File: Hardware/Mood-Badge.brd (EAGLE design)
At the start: 100 x 80 mm, 0 parts

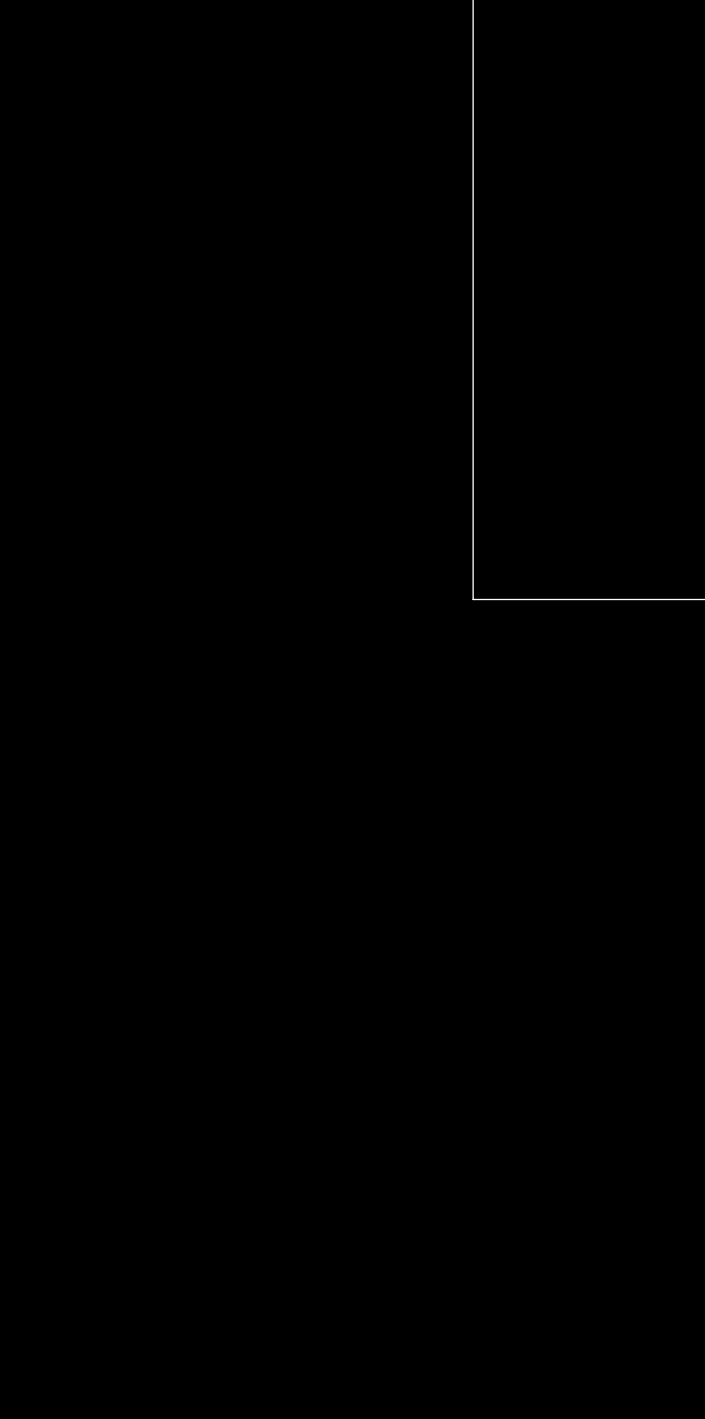
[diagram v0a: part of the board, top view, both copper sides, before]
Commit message: atmega schematics is now establish/included.
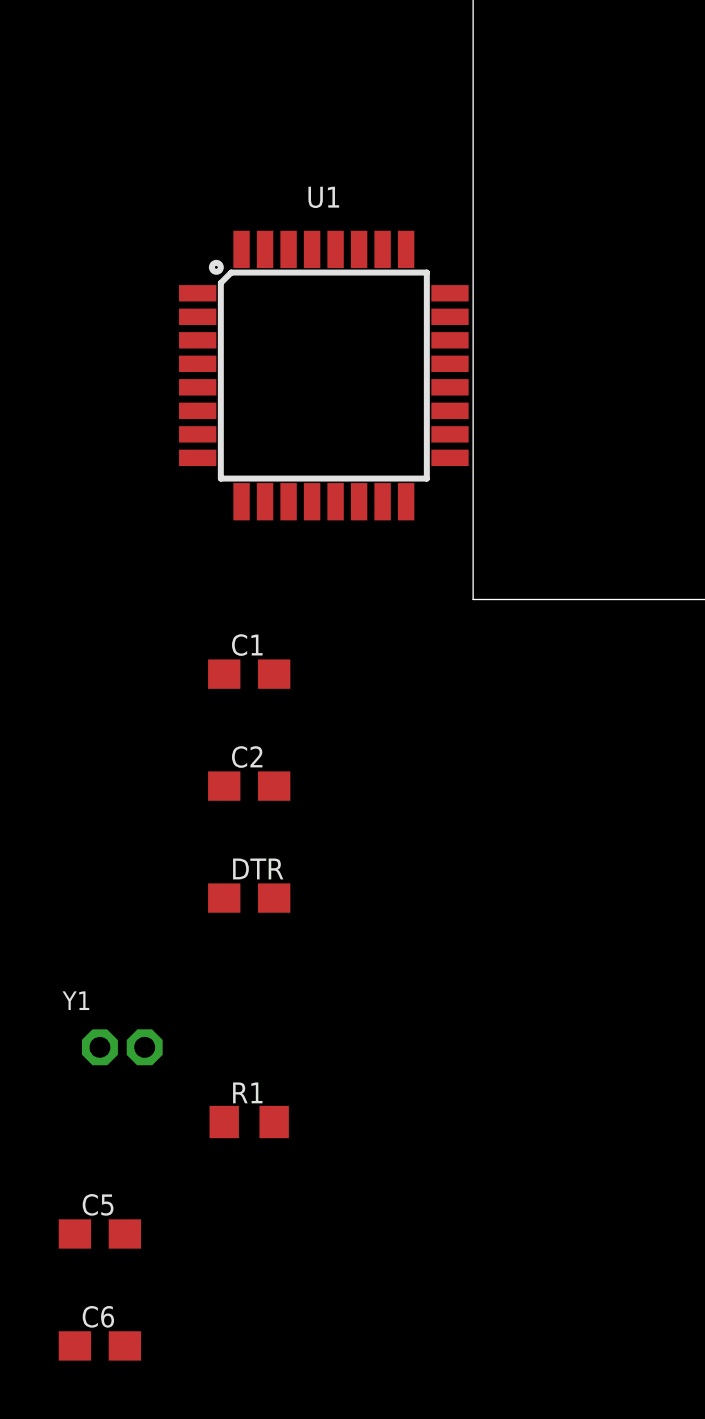
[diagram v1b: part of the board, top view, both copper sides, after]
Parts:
- added C1, C2, C5, C6, DTR: (no value), LinnesLab-Passives:C0603
- added R1: (no value), LinnesLab-Passives:R0603
- added U1: ATMEGA328P_TQFP, LinnesLab-Microcontrollers:TQFP32-08
- added Y1: (no value), LinnesLab-Clocks:CA-301
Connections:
- new net 3.3V: C5.1, C6.1, R1.2, U1.18, U1.4, U1.6
- new net ACTION: U1.19
- new net DTR: DTR.1
- new net GND: C1.2, C2.2, C5.2, C6.2, U1.21, U1.3, U1.5
- new net LD1: U1.2
- new net LD10: U1.16
- new net LD11: U1.15
- new net LD12: U1.14
- new net LD13: U1.13
- new net LD14: U1.12
- new net LD15: U1.11
- new net LD16: U1.10
- new net LD2: U1.1
- new net LD3: U1.32
- new net LD4: U1.28
- new net LD5: U1.27
- new net LD6: U1.26
- new net LD7: U1.25
- new net LD8: U1.24
- new net LD9: U1.17
- new net LEFT: U1.23
- new net MODE: U1.9
- new net N$1: C1.1, U1.8, Y1.1
- new net N$4: C2.1, U1.7, Y1.2
- new net RESET: DTR.2, R1.1, U1.29
- new net RIGHT: U1.22
- new net RXD: U1.30
- new net TXD: U1.31

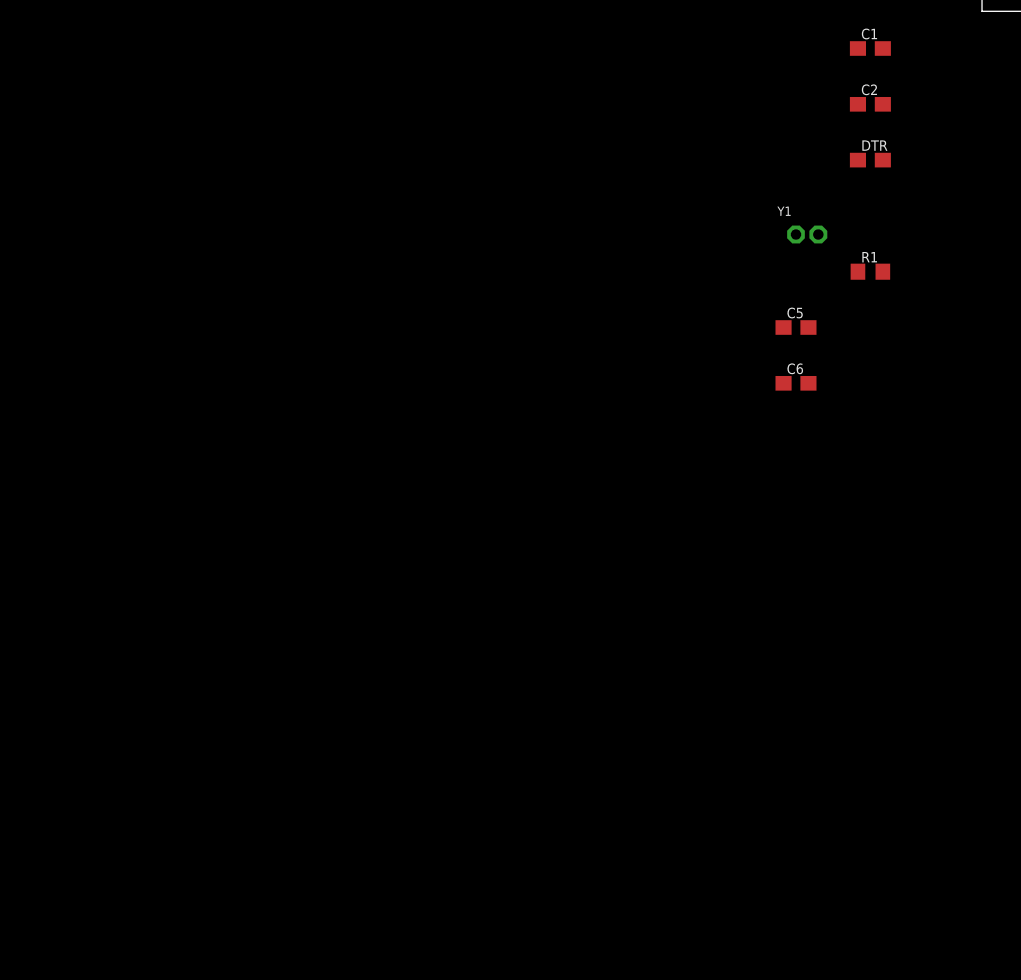
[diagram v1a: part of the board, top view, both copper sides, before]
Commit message: Power management circuit still in progress, bootload, ftdi, and LED matrix is done.
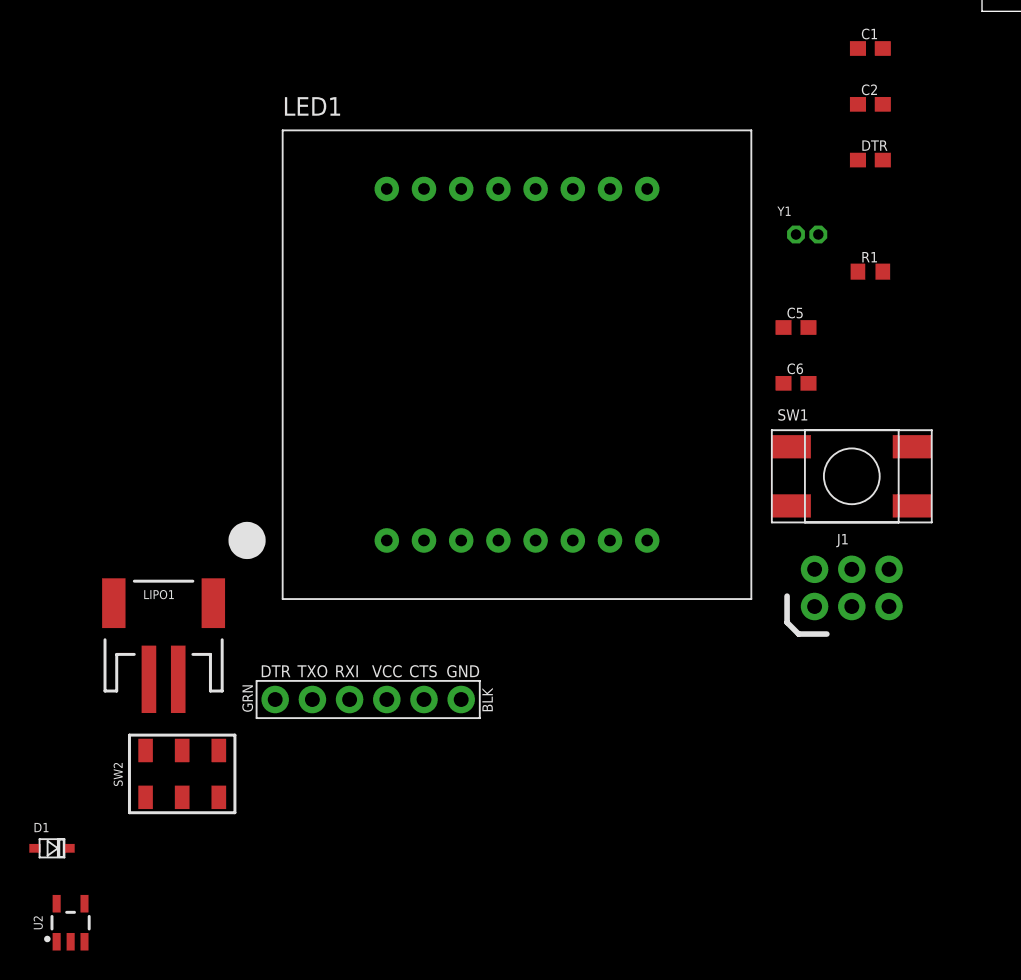
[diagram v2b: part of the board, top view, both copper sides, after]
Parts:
- added D1: (no value), LinnesLab-DiscreteSemi:USC
- added J1: AVR_SPI_PROG_3X2NS, LinnesLab-Connectors:2X3-NS
- added J2: FTDI_DEVICE, LinnesLab-Connectors:FTDI_DEVICE
- added LED1: (no value), LinnesLab-Displays:DOTMATRIX_BL-M12A881UR
- added LIPO1: (no value), LinnesLab-Connectors:JST-2-SMD
- added SW1: (no value), LinnesLab-Switches:SPST.KT11P4SM34LFS
- added SW2: SWITCH.JS202011JXQNUPWARDS, LinnesLab-Switches:SWITCH.00
- added U2: MIC550X, LinnesLab-Power:SOT23-5
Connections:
- new net N$2: LIPO1.2, SW2.2
- new net N$3: D1.+, SW2.1
- new net N$5: D1.-, U2.1
- net 3.3V: now also J1.2, J2.VCC
- net DTR: now also J2.DTR
- net GND: now also J1.6, J2.CTS, J2.GND, LIPO1.1, SW1.3, SW1.4
- net LD1: now also LED1.1
- net LD10: now also J1.1, LED1.10
- net LD11: now also J1.4, LED1.11
- net LD12: now also LED1.12
- net LD13: now also LED1.13
- net LD14: now also LED1.14
- net LD15: now also LED1.15
- net LD16: now also LED1.16
- net LD2: now also LED1.2
- net LD3: now also LED1.3
- net LD4: now also LED1.4
- net LD5: now also LED1.5
- net LD6: now also LED1.6
- net LD7: now also LED1.7
- net LD8: now also LED1.8
- net LD9: now also J1.3, LED1.9
- net RESET: now also J1.5, SW1.1, SW1.2
- net RXD: now also J2.RXI
- net TXD: now also J2.TXO
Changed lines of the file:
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@@
 <attribute name="VALUE" x="-13.335" y="-27.305" size="0.7112" layer="27"/>
+</element>
+<element name="SW1" library="LinnesLab-Switches" package="SPST.KT11P4SM34LFS" value="" x="-8.89" y="-31.75" smashed="yes">
+<attribute name="NAME" x="-13.97" y="-27.94" size="0.762" layer="25"/>
+<attribute name="VALUE" x="-13.97" y="-36.195" size="0.762" layer="27"/>
+</element>
+<element name="J1" library="LinnesLab-Connectors" package="2X3-NS" package3d_urn="urn:adsk.eagle:package:18167648/2" value="AVR_SPI_PROG_3X2NS" x="-8.89" y="-39.37" smashed="yes">
+<attribute name="NAME" x="-9.906" y="-36.3982" size="0.7112" layer="25" ratio="20"/>
+<attribute name="VALUE" x="-9.6774" y="-43.0276" size="0.7112" layer="27" ratio="20"/>
+</element>
+<element name="LED1" library="LinnesLab-Displays" package="DOTMATRIX_BL-M12A881UR" value="" x="-31.75" y="-24.13" smashed="yes">
+<attribute name="NAME" x="-47.75" y="-7.13" size="1.27" layer="25"/>
+<attribute name="VALUE" x="-47.75" y="-42.13" size="1.27" layer="27"/>
+</element>
+<element name="J2" library="LinnesLab-Connectors" package="FTDI_DEVICE" value="FTDI_DEVICE" x="-41.91" y="-46.99" smashed="yes"/>
+<element name="LIPO1" library="LinnesLab-Connectors" package="JST-2-SMD" value="" x="-55.88" y="-41.91" smashed="yes">
+<attribute name="NAME" x="-57.277" y="-40.132" size="0.6096" layer="25" ratio="20"/>
+<attribute name="PROD_ID" value="CONN-11443" x="-55.88" y="-41.91" size="1.778" layer="27" display="off"/>
+<attribute name="SF_ID" value="PRT-08612" x="-55.88" y="-41.91" size="1.778" layer="27" display="off"/>
+<attribute name="VALUE" x="-57.531" y="-41.275" size="0.6096" layer="27" ratio="20"/>
+</element>
+<element name="SW2" library="LinnesLab-Switches" package="SWITCH.00" value="SWITCH.JS202011JXQNUPWARDS" x="-54.61" y="-52.07" smashed="yes">
+<attribute name="NAME" x="-58.674" y="-52.0954" size="0.6096" layer="25" ratio="20" rot="R90" align="bottom-center"/>
+<attribute name="VALUE" x="-50.673" y="-52.07" size="0.6096" layer="27" ratio="20" rot="R90" align="top-center"/>
+</element>
+<element name="D1" library="LinnesLab-DiscreteSemi" package="USC" package3d_urn="urn:adsk.eagle:package:15664784/2" value="" x="-63.5" y="-57.15" smashed="yes">
+<attribute name="NAME" x="-64.77" y="-56.05" size="0.635" layer="25"/>
+<attribute name="VALUE" x="-64.77" y="-58.815" size="0.635" layer="27"/>
+</element>
+<element name="U2" library="LinnesLab-Power" package="SOT23-5" package3d_urn="urn:adsk.eagle:package:15662427/2" value="MIC550X" x="-62.23" y="-62.23" smashed="yes">
+<attribute name="NAME" x="-64.135" y="-62.23" size="0.6096" layer="25" ratio="20" rot="R90" align="bottom-center"/>
+<attribute name="VALUE" x="-59.69" y="-62.23" size="0.6096" layer="27" ratio="20" rot="R90" align="bottom-center"/>
 </element>
 </elements>
@@
 <contactref element="C6" pad="2"/>
 <contactref element="C5" pad="2"/>
+<contactref element="SW1" pad="3"/>
+<contactref element="SW1" pad="4"/>
+<contactref element="J1" pad="6"/>
+<contactref element="J2" pad="GND"/>
+<contactref element="J2" pad="CTS"/>
+<contactref element="LIPO1" pad="1"/>
+<wire x1="-38.1" y1="-46.99" x2="-56.88" y2="-45.61" width="0" layer="19" extent="1-1"/>
+<wire x1="-35.56" y1="-46.99" x2="-38.1" y2="-46.99" width="0" layer="19" extent="1-1"/>
+<wire x1="-13.0175" y1="-33.77" x2="-35.56" y2="-46.99" width="0" layer="19" extent="1-1"/>
+<wire x1="-6.35" y1="-38.1" x2="-13.0175" y2="-33.77" width="0" layer="19" extent="1-1"/>
+<wire x1="-4.7625" y1="-33.77" x2="-6.35" y2="-38.1" width="0" layer="19" extent="1-1"/>
+<wire x1="-11.85" y1="-25.4" x2="-13.0175" y2="-33.77" width="0" layer="19" extent="1-1"/>
 <wire x1="-11.85" y1="-21.59" x2="-11.85" y2="-25.4" width="0" layer="19" extent="1-1"/>
 <wire x1="-6.77" y1="-6.35" x2="-11.85" y2="-21.59" width="0" layer="19" extent="1-1"/>
@@
 <contactref element="U1" pad="29"/>
 <contactref element="R1" pad="1"/>
+<contactref element="SW1" pad="2"/>
+<contactref element="SW1" pad="1"/>
+<contactref element="J1" pad="5"/>
+<wire x1="-4.7625" y1="-29.73" x2="-6.35" y2="-40.64" width="0" layer="19" extent="1-1"/>
+<wire x1="-13.0175" y1="-29.73" x2="-4.7625" y2="-29.73" width="0" layer="19" extent="1-1"/>
+<wire x1="-8.47" y1="-17.78" x2="-4.7625" y2="-29.73" width="0" layer="19" extent="1-1"/>
 <wire x1="-6.77" y1="-10.16" x2="-8.47" y2="-17.78" width="0" layer="19" extent="1-1"/>
 <wire x1="-5.48" y1="11.9126" x2="-6.77" y2="-10.16" width="0" layer="19" extent="1-1"/>
@@
 <contactref element="C6" pad="1"/>
 <contactref element="C5" pad="1"/>
+<contactref element="J1" pad="2"/>
+<contactref element="J2" pad="VCC"/>
+<wire x1="-11.43" y1="-38.1" x2="-40.64" y2="-46.99" width="0" layer="19" extent="1-1"/>
+<wire x1="-13.55" y1="-25.4" x2="-11.43" y2="-38.1" width="0" layer="19" extent="1-1"/>
 <wire x1="-13.55" y1="-21.59" x2="-13.55" y2="-25.4" width="0" layer="19" extent="1-1"/>
 <wire x1="-6.77" y1="-17.78" x2="-13.55" y2="-21.59" width="0" layer="19" extent="1-1"/>
@@
 <signal name="DTR">
 <contactref element="DTR" pad="1"/>
+<contactref element="J2" pad="DTR"/>
+<wire x1="-8.47" y1="-10.16" x2="-48.26" y2="-46.99" width="0" layer="19" extent="1-1"/>
 </signal>
 <signal name="LEFT">
@@
 <signal name="LD8">
 <contactref element="U1" pad="24"/>
+<contactref element="LED1" pad="8"/>
+<wire x1="-0.7874" y1="10.42" x2="-22.86" y2="-36.13" width="0" layer="19" extent="1-1"/>
 </signal>
 <signal name="LD7">
 <contactref element="U1" pad="25"/>
+<contactref element="LED1" pad="7"/>
+<wire x1="-2.28" y1="11.9126" x2="-25.4" y2="-36.13" width="0" layer="19" extent="1-1"/>
 </signal>
 <signal name="LD6">
 <contactref element="U1" pad="26"/>
+<contactref element="LED1" pad="6"/>
+<wire x1="-3.08" y1="11.9126" x2="-27.94" y2="-36.13" width="0" layer="19" extent="1-1"/>
 </signal>
 <signal name="LD5">
 <contactref element="U1" pad="27"/>
+<contactref element="LED1" pad="5"/>
+<wire x1="-3.88" y1="11.9126" x2="-30.48" y2="-36.13" width="0" layer="19" extent="1-1"/>
 </signal>
 <signal name="LD4">
 <contactref element="U1" pad="28"/>
+<contactref element="LED1" pad="4"/>
+<wire x1="-4.68" y1="11.9126" x2="-33.02" y2="-36.13" width="0" layer="19" extent="1-1"/>
 </signal>
 <signal name="ACTION">
@@
 <signal name="RXD">
 <contactref element="U1" pad="30"/>
+<contactref element="J2" pad="RXI"/>
+<wire x1="-6.28" y1="11.9126" x2="-43.18" y2="-46.99" width="0" layer="19" extent="1-1"/>
 </signal>
 <signal name="TXD">
 <contactref element="U1" pad="31"/>
+<contactref element="J2" pad="TXO"/>
+<wire x1="-7.08" y1="11.9126" x2="-45.72" y2="-46.99" width="0" layer="19" extent="1-1"/>
 </signal>
 <signal name="LD3">
 <contactref element="U1" pad="32"/>
+<contactref element="LED1" pad="3"/>
+<wire x1="-7.88" y1="11.9126" x2="-35.56" y2="-36.13" width="0" layer="19" extent="1-1"/>
 </signal>
 <signal name="LD2">
 <contactref element="U1" pad="1"/>
+<contactref element="LED1" pad="2"/>
+<wire x1="-9.3726" y1="10.42" x2="-38.1" y2="-36.13" width="0" layer="19" extent="1-1"/>
 </signal>
 <signal name="LD1">
 <contactref element="U1" pad="2"/>
+<contactref element="LED1" pad="1"/>
+<wire x1="-9.3726" y1="9.62" x2="-40.64" y2="-36.13" width="0" layer="19" extent="1-1"/>
 </signal>
 <signal name="MODE">
@@
 <signal name="LD16">
 <contactref element="U1" pad="10"/>
+<contactref element="LED1" pad="16"/>
+<wire x1="-7.08" y1="3.3274" x2="-40.64" y2="-12.13" width="0" layer="19" extent="1-1"/>
 </signal>
 <signal name="LD15">
 <contactref element="U1" pad="11"/>
+<contactref element="LED1" pad="15"/>
+<wire x1="-6.28" y1="3.3274" x2="-38.1" y2="-12.13" width="0" layer="19" extent="1-1"/>
 </signal>
 <signal name="LD14">
 <contactref element="U1" pad="12"/>
+<contactref element="LED1" pad="14"/>
+<wire x1="-5.48" y1="3.3274" x2="-35.56" y2="-12.13" width="0" layer="19" extent="1-1"/>
 </signal>
 <signal name="LD13">
 <contactref element="U1" pad="13"/>
+<contactref element="LED1" pad="13"/>
+<wire x1="-4.68" y1="3.3274" x2="-33.02" y2="-12.13" width="0" layer="19" extent="1-1"/>
 </signal>
 <signal name="LD12">
 <contactref element="U1" pad="14"/>
+<contactref element="LED1" pad="12"/>
+<wire x1="-3.88" y1="3.3274" x2="-30.48" y2="-12.13" width="0" layer="19" extent="1-1"/>
 </signal>
 <signal name="LD11">
 <contactref element="U1" pad="15"/>
+<contactref element="J1" pad="4"/>
+<contactref element="LED1" pad="11"/>
+<wire x1="-27.94" y1="-12.13" x2="-8.89" y2="-38.1" width="0" layer="19" extent="1-1"/>
+<wire x1="-3.08" y1="3.3274" x2="-27.94" y2="-12.13" width="0" layer="19" extent="1-1"/>
 </signal>
 <signal name="LD10">
 <contactref element="U1" pad="16"/>
+<contactref element="J1" pad="1"/>
+<contactref element="LED1" pad="10"/>
+<wire x1="-25.4" y1="-12.13" x2="-11.43" y2="-40.64" width="0" layer="19" extent="1-1"/>
+<wire x1="-2.28" y1="3.3274" x2="-25.4" y2="-12.13" width="0" layer="19" extent="1-1"/>
 </signal>
 <signal name="LD9">
 <contactref element="U1" pad="17"/>
+<contactref element="J1" pad="3"/>
+<contactref element="LED1" pad="9"/>
+<wire x1="-22.86" y1="-12.13" x2="-8.89" y2="-40.64" width="0" layer="19" extent="1-1"/>
+<wire x1="-0.7874" y1="4.82" x2="-22.86" y2="-12.13" width="0" layer="19" extent="1-1"/>
+</signal>
+<signal name="N$2">
+<contactref element="LIPO1" pad="2"/>
+<contactref element="SW2" pad="2"/>
+<wire x1="-54.88" y1="-45.61" x2="-54.61" y2="-50.47" width="0" layer="19" extent="1-1"/>
+</signal>
+<signal name="N$3">
+<contactref element="SW2" pad="1"/>
+<contactref element="D1" pad="+"/>
+<wire x1="-57.11" y1="-50.47" x2="-64.65" y2="-57.15" width="0" layer="19" extent="1-1"/>
+</signal>
+<signal name="N$5">
+<contactref element="D1" pad="-"/>
+<contactref element="U2" pad="1"/>
+<wire x1="-62.35" y1="-57.15" x2="-63.18" y2="-63.5301" width="0" layer="19" extent="1-1"/>
 </signal>
 </signals>
